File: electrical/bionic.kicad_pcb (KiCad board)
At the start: 2 copper layers, 100 x 75 mm, 37 parts, among them J1 PWR, M1 N20, M2 N20, M3 N20, M4 N20, M5 N20, M6 N20, M7 N20, SW1 SW_SPST, U1 ESP32, U2 SAMD09, U3 CD4069, U4 CD4069, U5 LM338

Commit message: update(electrical/pcb): signal wiring Complete!!
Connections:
- D4 pad 10: /PWM7 -> unconnected-(D4-PWMB-Pad10)
- D4 pad 11: /M7B -> unconnected-(D4-BI2-Pad11)
- D4 pad 12: /DIR7 -> unconnected-(D4-BI1-Pad12)
- D4 pad 14: unconnected-(D4-AI1-Pad14) -> /DIR7
- D4 pad 15: unconnected-(D4-AI2-Pad15) -> /M7B
- D4 pad 16: unconnected-(D4-PWMA-Pad16) -> /PWM7
- D4 pad 4: unconnected-(D4-A01-Pad4) -> /M7+
- D4 pad 5: unconnected-(D4-A02-Pad5) -> /M7-
- D4 pad 6: /M7+ -> unconnected-(D4-B01-Pad6)
- D4 pad 7: /M7- -> unconnected-(D4-B02-Pad7)
- U1 pad 10: /ENA7 -> /PWM6
- U1 pad 15: /ENB7 -> /PWM5
- U1 pad 22: /ENB1 -> /ENA1
- U1 pad 23: /ENA1 -> /ENB1
- U1 pad 3: /PWM5 -> /ENB7
- U1 pad 4: /ENA5 -> /ENA7
- U1 pad 5: /ENB5 -> /ENB6
- U1 pad 6: /PWM6 -> /ENA6
- U1 pad 7: /ENA6 -> /ENB5
- U1 pad 8: /ENB6 -> /ENA5
- U2 pad 11: /DIR4 -> /DIR2
- U2 pad 12: /DIR5 -> /DIR1
- U2 pad 8: /DIR1 -> /DIR5
- U2 pad 9: /DIR2 -> /DIR4
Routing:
- net /PWM5: track 0.00 -> 102.9 mm
- net /ENA5: track 0.00 -> 96.8 mm
- net /ENB5: track 0.00 -> 91.4 mm
- net /PWM6: track 0.00 -> 74.6 mm
- net /ENA6: track 0.00 -> 73.2 mm
- net /DIR5: track 0.00 -> 71.7 mm
- net /ENB6: track 0.00 -> 67.8 mm
- net /DIR4: track 0.00 -> 66.7 mm
- net /PWM7: track 0.00 -> 66.6 mm
- net /DIR3: track 0.00 -> 59.5 mm
- net /DIR6: track 0.00 -> 57.0 mm
- net /SCL: track 0.00 -> 44.0 mm
- net /DIR2: track 0.00 -> 43.6 mm
- net /DIR7: track 0.00 -> 42.1 mm
- net /DIR1: track 0.00 -> 37.4 mm
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
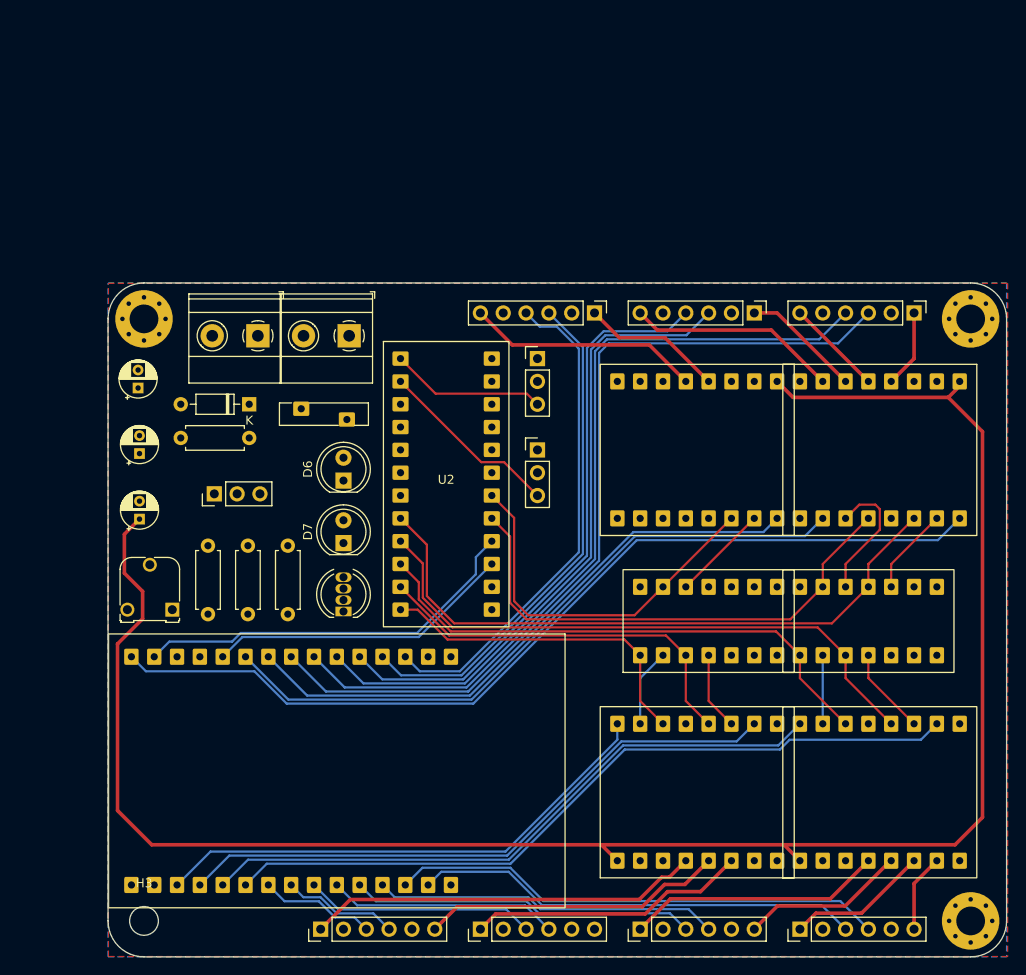
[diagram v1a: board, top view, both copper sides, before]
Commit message: update(electrical/pcb): DRC Passed! and Updated 3D-Models
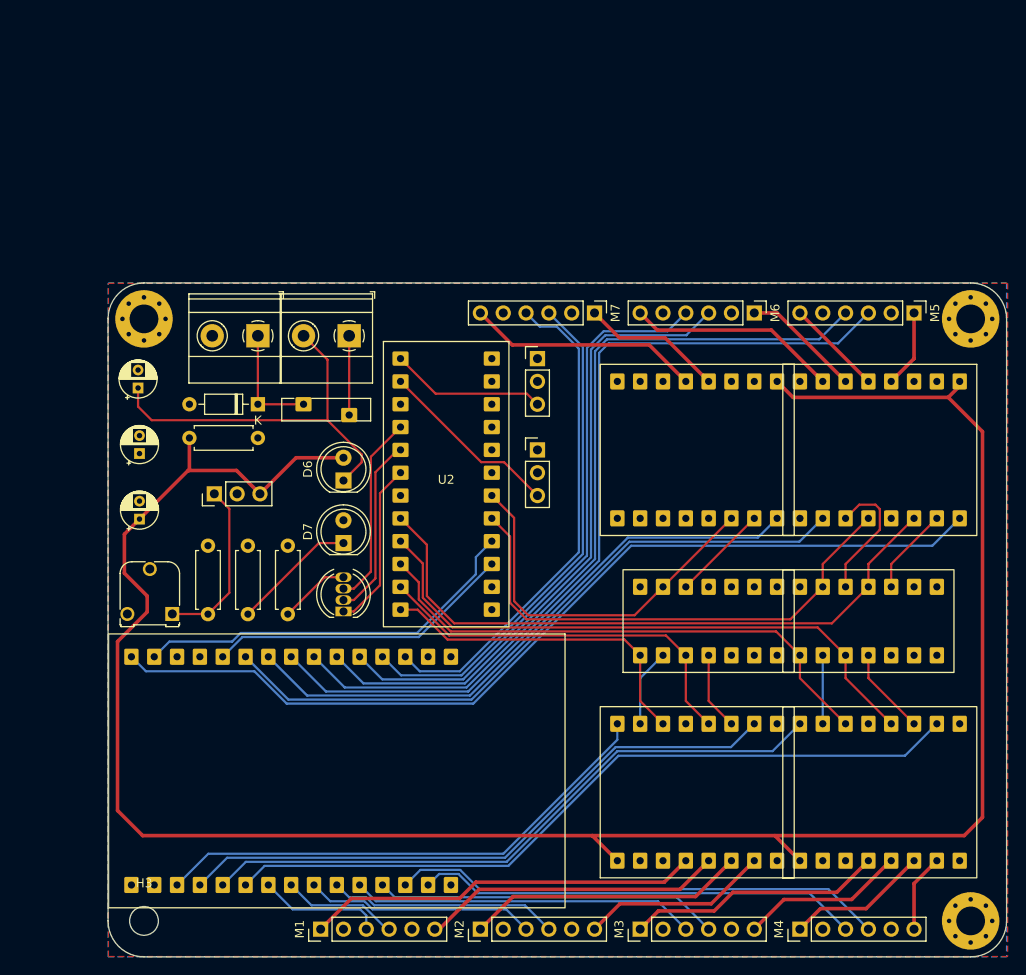
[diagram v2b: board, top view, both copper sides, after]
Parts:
- M1, M2, M3, M4, M5, M6, M7: footprint Connector_PinHeader_2.54mm:PinHeader_1x06_P2.54mm_Vertical -> bionic:JST_1x06_P2.54mm_Vertical
- moved D5 0.97 mm to (66.7, 63.5)
- moved R1 0.96 mm to (59.1, 67.2)
- moved F1 0.56 mm to (71.8, 63.5)
- moved RV1 0.48 mm to (57.1, 86.8)
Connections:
- U2 pad 4: /L_RED -> /L_BLU
- U2 pad 6: /L_BLU -> /L_RED
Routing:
- net Net-(D6-K): track 0.00 -> 43.4 mm
- net /+6V: track 209.7 -> 243.4 mm
- net /L_BLU: track 0.00 -> 21.3 mm
- net /M2-: track 0.00 -> 20.9 mm
- net /L_GRN: track 0.00 -> 20.2 mm
- net Net-(U5-ADJ): track 0.00 -> 19.5 mm
- net /L_RED: track 0.00 -> 18.7 mm
- net Net-(D7-K): track 0.00 -> 14.3 mm
- net Net-(D5-K): track 0.00 -> 12.7 mm
- net Net-(SW1-A): track 0.00 -> 9.18 mm
- net Net-(D8-A): track 0.00 -> 8.32 mm
- net /ENA1: track 12.9 -> 13.8 mm
- added copper zone on B.Cu, net /+3V3
- added copper zone on F.Cu, net GND
- removed copper zone on F.Cu, net /+3V3
- removed copper zone on B.Cu, net GND

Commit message: update(electrical/pcb): Updated Placement and Reduce Board
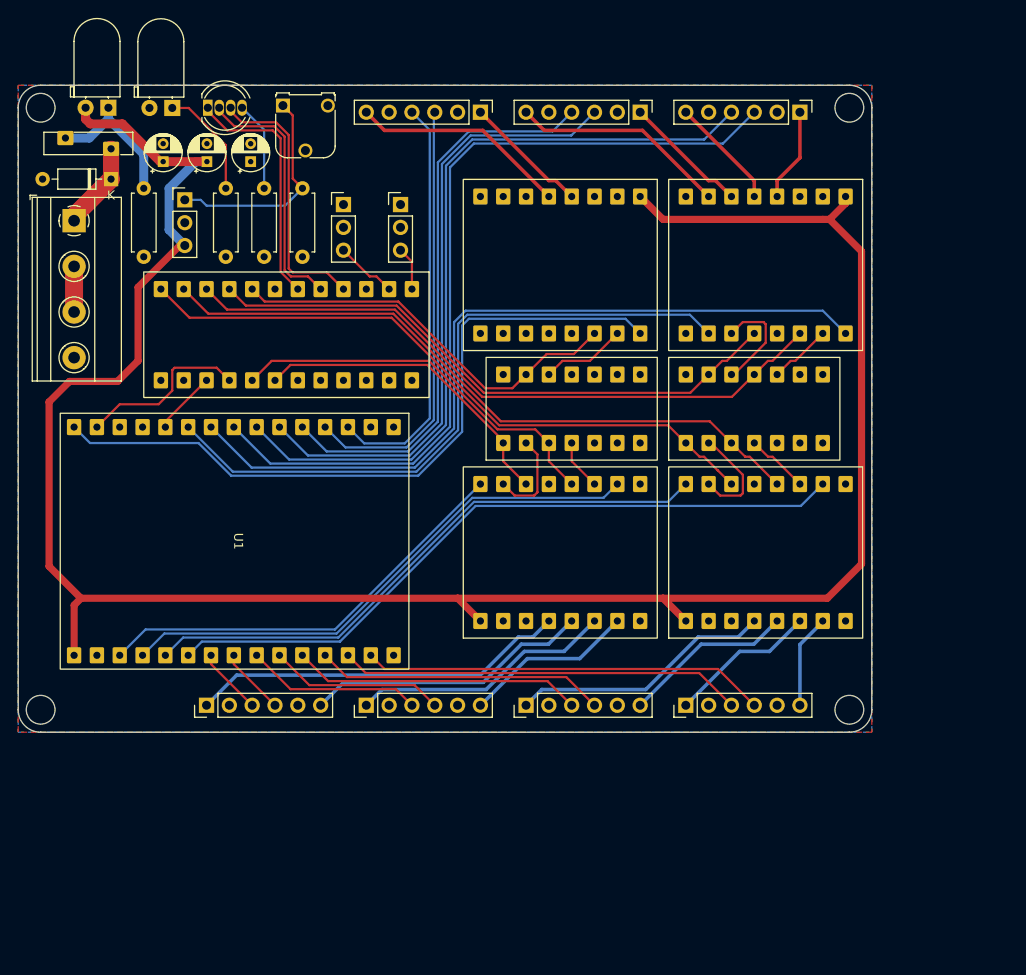
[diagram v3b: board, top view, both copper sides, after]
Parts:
- removed SW1: SW_SPST, TerminalBlock_Phoenix:TerminalBlock_Phoenix_MKDS-1,5-2-5.08_1x02_P5.08mm_Horizontal
- D6, D7: footprint LED_THT:LED_D5.0mm -> LED_THT:LED_D5.0mm_Horizontal_O1.27mm_Z3.0mm
- H1, H2, H4: value MountingHole_Pad -> MountingHole; footprint MountingHole:MountingHole_3.2mm_M3_Pad_Via -> MountingHole:MountingHole_3.2mm_M3
- J1: value PWR -> Screw_Terminal_01x04; footprint TerminalBlock_Phoenix:TerminalBlock_Phoenix_MKDS-1,5-2-5.08_1x02_P5.08mm_Horizontal -> TerminalBlock_Phoenix:TerminalBlock_Phoenix_MKDS-1,5-4-5.08_1x04_P5.08mm_Horizontal
- S1, S2: footprint Connector_PinHeader_2.54mm:PinHeader_1x03_P2.54mm_Vertical -> bionic:JST_1x03_P2.54mm_Vertical
- moved H4 106.1 mm to (42.5, 97.5)
- moved H3 81.9 mm to (132.5, 97.5)
- moved D8 58.1 mm to (61.1, 30.5), turned to 0 degrees
- moved RV1 57.9 mm to (69.5, 30.3), turned to 0 degrees
- moved D7 52.0 mm to (57.1, 30.5), turned to 180 degrees
- moved D6 49.1 mm to (50.0, 30.5), turned to 180 degrees
- moved R3 47.5 mm to (63.1, 39.5), turned to -90 degrees
- moved C2 40.5 mm to (61.0, 36.5)
- moved F1 35.6 mm to (50.3, 35.1), turned to 180 degrees
- moved C3 34.8 mm to (65.9, 36.5)
- moved R2 33.8 mm to (71.6, 47.1), turned to 90 degrees
- moved U5 32.9 mm to (58.5, 40.8), turned to 0 degrees
- moved R4 32.3 mm to (67.4, 47.1), turned to 90 degrees
- moved S2 31.3 mm to (82.5, 41.3)
- moved D1 30.7 mm to (100.3, 80.0)
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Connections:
- C1 pad 1: Net-(D6-K) -> /+6V
- F1 pad 2: Net-(SW1-A) -> Net-(D6-K)
- J1 pad 2: GND -> Net-(J1-Pin_2)
- R1 pad 1: /+6V -> Net-(D6-K)
- U1 pad 15: /PWM5 -> /PWM7
- U1 pad 16: /+3V3 -> /+6V
- U1 pad 28: /ENB4 -> /ENA4
- U1 pad 29: /ENA4 -> /ENB4
- U1 pad 9: /PWM7 -> /PWM5
- U2 pad 1: /EMG1 -> /EMG2
- U2 pad 10: /DIR3 -> /DIR5
- U2 pad 11: /DIR2 -> /DIR4
- U2 pad 12: /DIR1 -> /DIR3
- U2 pad 17: /DIR6 -> /DIR2
- U2 pad 18: /DIR7 -> /DIR1
- U2 pad 2: /EMG2 -> /EMG1
- U2 pad 8: /DIR5 -> /DIR7
- U2 pad 9: /DIR4 -> /DIR6
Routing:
- net /SDA: track 34.2 -> 7.09 mm
- net Net-(D6-K): track 43.4 -> 17.5 mm
- net /SCL: track 44.0 -> 19.4 mm
- net /EMG2: track 20.5 -> 4.85 mm
- net /PWM5: track 103.1 -> 87.7 mm
- net /PWM7: track 66.6 -> 80.1 mm
- net /DIR3: track 59.5 -> 72.5 mm
- net /EMG1: track 17.3 -> 6.87 mm
- net /ENB4: track 55.0 -> 45.0 mm
- net /ENB7: track 55.7 -> 45.9 mm
- net /PWM1: track 57.5 -> 48.0 mm
- net Net-(SW1-A): track 9.18 -> 0.00 mm
- net /DIR6: track 57.0 -> 65.9 mm
- net /L_BLU: track 21.3 -> 30.0 mm
- net /L_RED: track 18.7 -> 27.3 mm
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- added copper zone on F.Cu, net /+3V3
- added copper zone on B.Cu, net GND
- removed copper zone on B.Cu, net /+3V3
- removed copper zone on F.Cu, net GND
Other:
- board size 100 x 75 mm -> 95 x 72 mm

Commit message: update(electrical/pcb): Finialized v1.0 Design
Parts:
- removed D5: D_Small, Diode_THT:D_DO-35_SOD27_P7.62mm_Horizontal
- removed D6, D7: LED_Small, LED_THT:LED_D5.0mm_Horizontal_O1.27mm_Z3.0mm
- removed D8: LED_RGBA, LED_THT:LED_D5.0mm-4_RGB
- added G***: LOGO, LOGO, B.Cu at (51.0, 79.6)
- added MD1: TB6612, bionic:TB6612, F.Cu at (100.3, 80.0)
- added MD2: TB6612, bionic:TB6612, F.Cu at (123.2, 80.0)
- added MD3: TB6612, bionic:TB6612, F.Cu at (123.2, 48.0)
- added MD4: TB6612, bionic:TB6612, F.Cu at (100.3, 48.0)
- added REF**: KiCad-Logo2_5mm_SilkScreen, Symbol:KiCad-Logo2_5mm_SilkScreen, B.Cu at (66.6, 78.5)
- added T1: TestPoint_Probe, TestPoint:TestPoint_Pad_1.0x1.0mm, F.Cu at (48.8, 97.0)
- D1: value TB6612 -> D_Small; footprint bionic:TB6612 -> Diode_THT:D_DO-35_SOD27_P7.62mm_Horizontal
- D2, D3: value TB6612 -> LED_Small; footprint bionic:TB6612 -> LED_THT:LED_D5.0mm_Horizontal_O1.27mm_Z3.0mm
- D4: value TB6612 -> LED_RGBA; footprint bionic:TB6612 -> LED_THT:LED_D5.0mm-4_RGB
- moved D2 88.3 mm to (50.0, 30.5), turned to 180 degrees
- moved D3 68.3 mm to (57.1, 30.5), turned to 180 degrees
- moved D1 65.0 mm to (50.3, 38.4), turned to 180 degrees
- moved D4 43.0 mm to (61.1, 30.5), turned to 0 degrees
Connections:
- D1 pad 1: /+6V -> Net-(D1-K)
- D1 pad 2: /+3V3 -> GND
- D2 pad 1: /+6V -> Net-(D2-K)
- D2 pad 2: /+3V3 -> /+6V
- D3 pad 1: /+6V -> Net-(D3-K)
- D4 pad 1: /+6V -> /L_RED
- D4 pad 2: /+3V3 -> /L_GRN
- D4 pad 3: GND -> /L_BLU
- D4 pad 4: /M7+ -> Net-(D4-A)
- F1 pad 1: Net-(D5-K) -> Net-(D1-K)
- F1 pad 2: Net-(D6-K) -> Net-(D2-K)
- J1 pad 1: Net-(D5-K) -> Net-(D1-K)
- R1 pad 1: Net-(D6-K) -> Net-(D2-K)
- R3 pad 1: Net-(D7-K) -> Net-(D3-K)
- R4 pad 2: Net-(D8-A) -> Net-(D4-A)
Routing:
- net Net-(D6-K): track 17.5 -> 0.00 mm
- net Net-(D2-K): track 0.00 -> 17.5 mm
- net Net-(D7-K): track 12.5 -> 0.00 mm
- net Net-(D3-K): track 0.00 -> 12.5 mm
- net Net-(D8-A): track 9.99 -> 0.00 mm
- net Net-(D4-A): track 0.00 -> 9.99 mm
- net Net-(D5-K): track 9.70 -> 0.00 mm
- net Net-(D1-K): track 0.00 -> 9.70 mm
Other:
- board text added: "+3V3"
- board text added: "BionicBoard"
- board text added: "Designed by:"
- board text added: "Shrijal"
- board text added: "Team RED"
- board text added: "V1.0"
